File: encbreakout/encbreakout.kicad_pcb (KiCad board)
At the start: 2 copper layers, 50 x 50 mm, 3 parts, among them J1 Conn_01x09, U1 AS5047

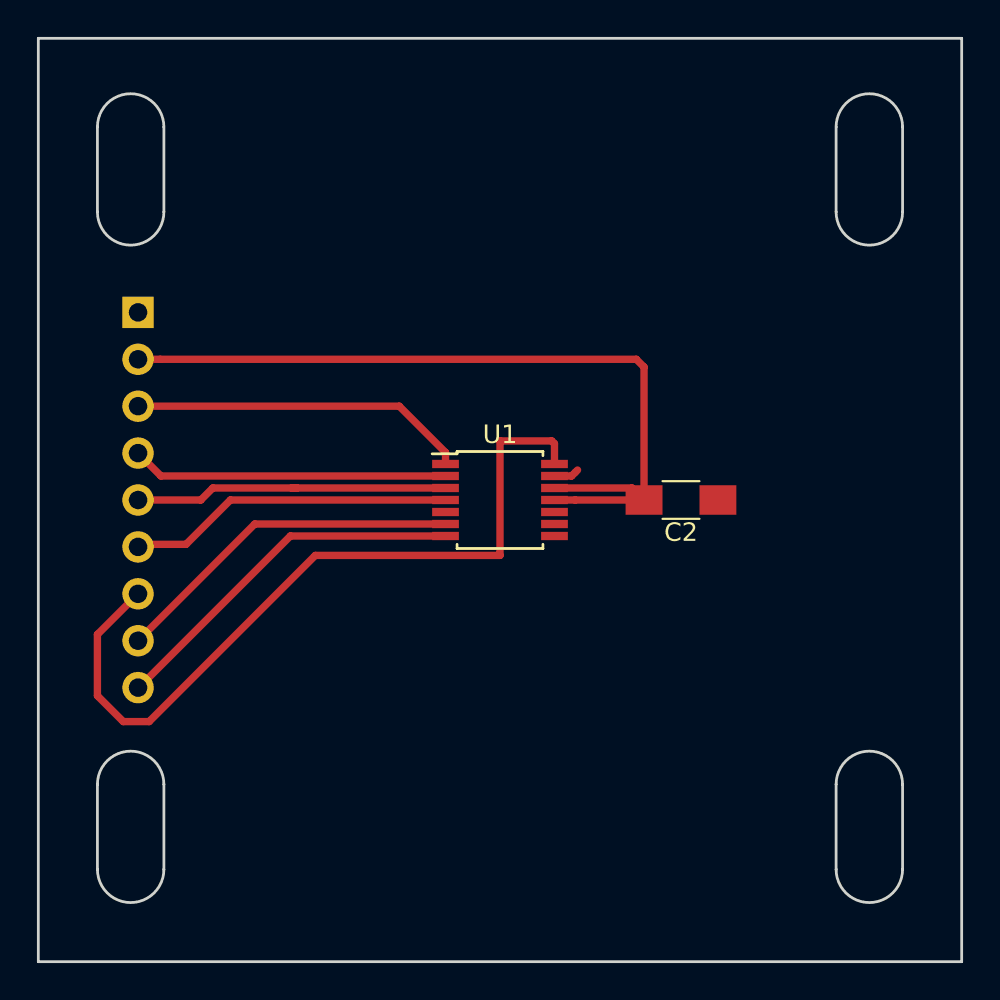
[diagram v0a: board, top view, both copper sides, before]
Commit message: encbreakout: add silk
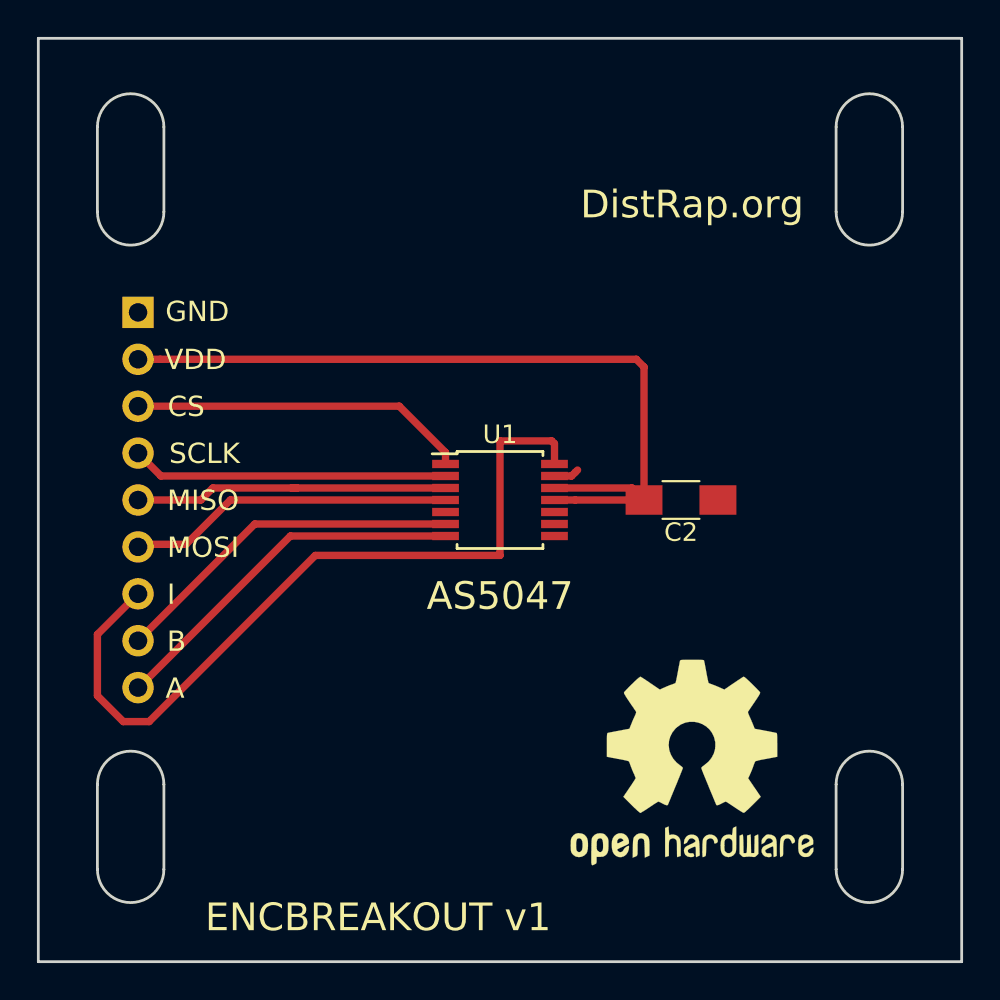
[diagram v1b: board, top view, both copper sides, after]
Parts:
- added REF***: OSHW-Logo2_14.6x12mm_SilkScreen, Symbols:OSHW-Logo2_14.6x12mm_SilkScreen, F.Cu at (169.4, 133.2)
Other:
- board text added: "A"
- board text added: "AS5047"
- board text added: "B"
- board text added: "CS"
- board text added: "DistRap.org"
- board text added: "ENCBREAKOUT v1"
- board text added: "GND"
- board text added: "I"
- board text added: "MISO"
- board text added: "MOSI"
- board text added: "SCLK"
- board text added: "VDD"

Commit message: update encbreakout
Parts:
- added G***: LOGO, libs:distrap_logo_mini_9x9mm, B.Cu at (168.5, 103.0)
- added G***: LOGO, libs:distrap_logo_mini_9x9mm, F.Cu at (168.5, 103.0)
- added REF***: OSHW-Logo2_14.6x12mm_SilkScreen, Symbols:OSHW-Logo2_14.6x12mm_SilkScreen, B.Cu at (169.4, 133.2)
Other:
- board text removed: "DistRap.org"
